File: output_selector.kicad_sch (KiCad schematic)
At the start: 0 parts

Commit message: power supply first draft
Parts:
- added U2: ATTINY9-TS8R, 0__:SOT95P270X145-6N, symbol 0 __:ATTINY9-TS8R
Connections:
- new net +5V: U2.5 (VCC)
- new net GND: U2.2 (GND)

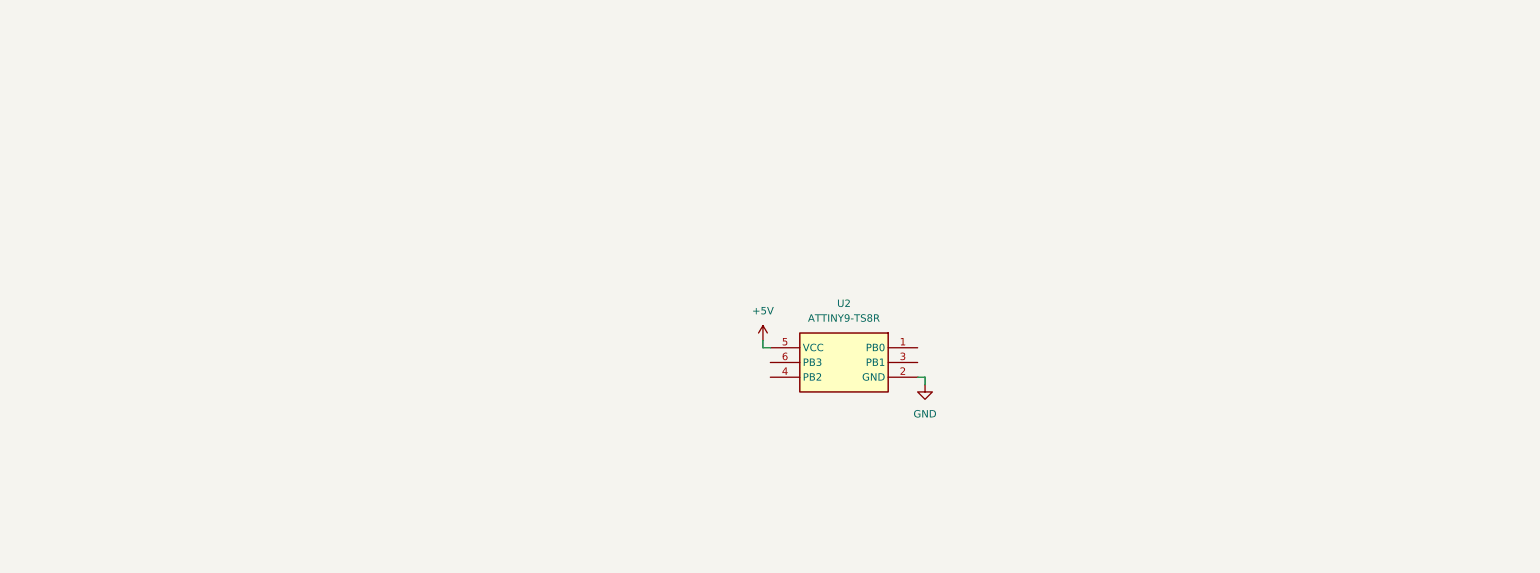
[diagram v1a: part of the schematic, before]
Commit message: Add output selector
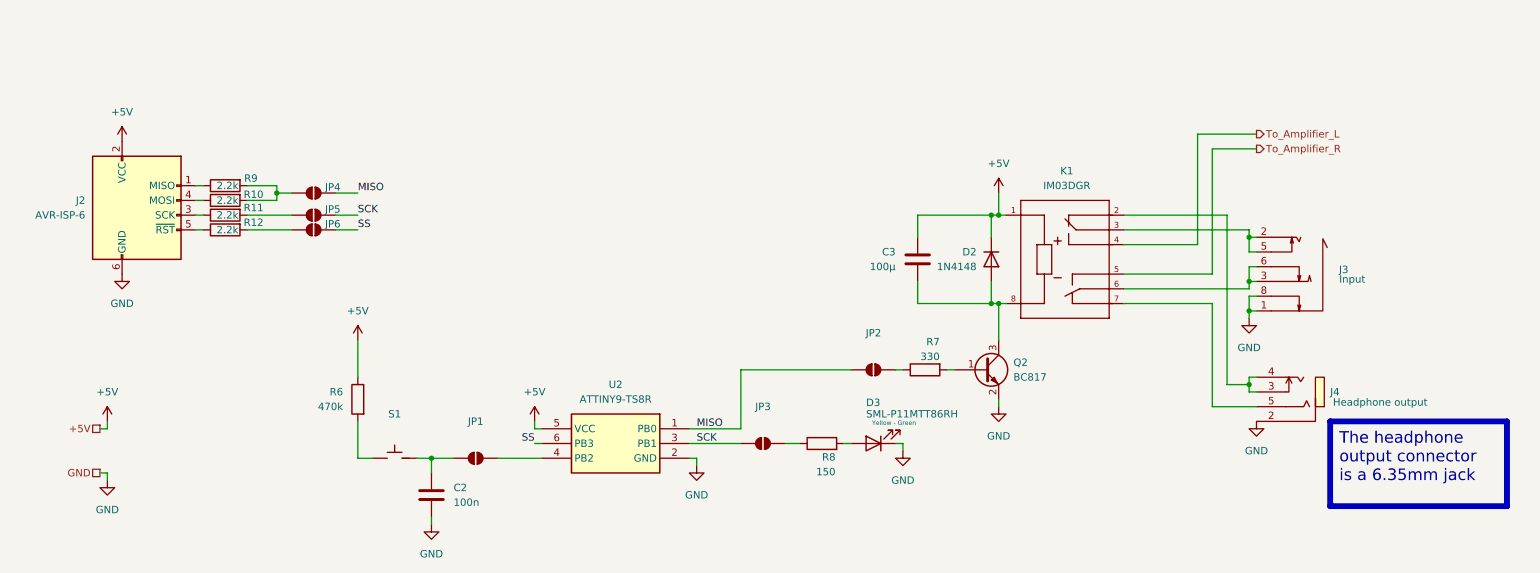
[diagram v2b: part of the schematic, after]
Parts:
- added C2: 100n, symbol Device:C
- added C3: 100µ, symbol Device:C
- added D2: 1N4148, Diode_THT:D_DO-35_SOD27_P7.62mm_Horizontal, symbol Diode:1N4148
- added D3: SML-P11MTT86RH, LED_SMD:LED_0402_1005Metric, symbol Device:LED
- added J2: AVR-ISP-6, symbol Connector:AVR-ISP-6
- added J3: PJ-393-8P, 0__:AUDIO-TH_PJ-393-8A, symbol 0 __:PJ-393-8P
- added J4: PJ-603, 0__:AUDIO-TH_PJ-603, symbol 0 __:PJ-603
- added JP1, JP2, JP3, JP4, JP5, JP6: SolderJumper_2_Open, Jumper:SolderJumper-2_P1.3mm_Open_TrianglePad1.0x1.5mm, symbol Jumper:SolderJumper_2_Open
- added K1: IM03DGR, 0__:RELAY_IM03DGR, symbol 0 __:IM03DGR
- added Q2: BC817, Package_TO_SOT_SMD:SOT-23, symbol Transistor_BJT:BC817
- added R10, R11, R12, R9: 2.2k, symbol Device:R
- added R6: 470k, symbol Device:R
- added R7: 330, symbol Device:R
- added R8: 150, symbol Device:R
- added S1: PG151101S11, 0__:SW_PG151101S11, symbol 0 __:PG151101S11
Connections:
- net +5V: now also C3.2, D2.1 (K), J2.2 (VCC), K1.1, R6.1
- net GND: now also C2.1, D3.1 (K), J2.6 (GND), J3.1, J3.8, J4.2, Q2.2 (E)
- net MISO: now reaches U2.1 (PB0)
- net MISO: now also JP2.1 (A), JP4.2 (B)
- net SCK: now reaches U2.3 (PB1)
- net SCK: now also JP3.1 (A), JP5.2 (B)
- net at U2.4 (PB2): now also JP1.2 (B)
- net SS: now reaches U2.6 (PB3)
- net SS: now also JP6.2 (B)
- new net: JP5.1 (A), R11.2
- new net: JP6.1 (A), R12.2
- new net: JP4.1 (A), R10.2, R9.2
- new net: C2.2, JP1.1 (A), S1.2
- new net: JP3.2 (B), R8.1
- new net: C3.1, D2.2 (A), K1.8, Q2.3 (C)
- new net: JP2.2 (B), R7.1
- new net: J2.4 (MOSI), R10.1
- new net: D3.2 (A), R8.2
- new net: Q2.1 (B), R7.2
- new net: J4.3, J4.4, K1.2
- new net: J3.2, J3.5, K1.3
- new net: J3.3, J3.6, K1.6
- new net: J4.5, K1.7
- new net: R6.2, S1.1
- new net: J2.3 (SCK), R11.1
- new net: J2.5 (~{RST}), R12.1
- new net: J2.1 (MISO), R9.1
- new net To_Amplifier_L: K1.4
- new net To_Amplifier_R: K1.5
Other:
- moved on the sheet: U2

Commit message: draft amplifier circuit
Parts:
- added JP7: SolderJumper_2_Open, Jumper:SolderJumper-2_P1.3mm_Open_TrianglePad1.0x1.5mm, symbol Jumper:SolderJumper_2_Open
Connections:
- net SS: now also JP7.2 (B)
- new net ~{AmpSD}: JP7.1 (A)
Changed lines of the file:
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@@
+	(wire
+		(pts
+			(xy 137.16 158.75) (xy 140.97 158.75)
+		)
+		(stroke
+			(width 0)
+			(type default)
+		)
+	)
 	(wire
 		(pts
@@
 	(wire
 		(pts
+			(xy 129.54 158.75) (xy 128.27 158.75)
+		)
+		(stroke
+			(width 0)
+			(type default)
+		)
+	)
+	(wire
+		(pts
 			(xy 66.04 154.94) (xy 66.04 156.21)
 		)
@@
 		(pts
 			(xy 219.71 134.62) (xy 219.71 140.97)
-		)
-		(stroke
-			(width 0)
-			(type default)
-		)
-	)
-	(wire
-		(pts
-			(xy 139.7 158.75) (xy 140.97 158.75)
 		)
 		(stroke
@@
 		(shape passive)
 		(at 64.77 163.83 180)
+		(fields_autoplaced yes)
+		(effects
+			(font
+				(size 1.27 1.27)
+			)
+			(justify right)
+		)
+	)
+	(hierarchical_label "~{AmpSD}"
+		(shape output)
+		(at 128.27 158.75 180)
 		(fields_autoplaced yes)
 		(effects
@@
 		(on_board yes)
 		(dnp no)
-		(fields_autoplaced yes)
 		(property "Reference" "JP1"
-			(at 129.54 154.94 0)
+			(at 129.54 163.576 0)
 			(effects
 				(font
@@
 					(unit 1)
 				)
+			)
+		)
+	)
+	(symbol
+		(lib_id "Jumper:SolderJumper_2_Open")
+		(at 133.35 158.75 0)
+		(unit 1)
+		(exclude_from_sim yes)
+		(in_bom no)
+		(on_board yes)
+		(dnp no)
+		(property "Reference" "JP7"
+			(at 133.35 156.21 0)
+			(effects
+				(font
+					(size 1.27 1.27)
+				)
+			)
+		)
+		(property "Value" "SolderJumper_2_Open"
+			(at 133.35 154.94 0)
+			(effects
+				(font
+					(size 1.27 1.27)
+				)
+				(hide yes)
+			)
+		)
+		(property "Footprint" "Jumper:SolderJumper-2_P1.3mm_Open_TrianglePad1.0x1.5mm"
+			(at 133.35 158.75 0)
+			(effects
+				(font
+					(size 1.27 1.27)
+				)
+				(hide yes)
+			)
+		)
+		(property "Datasheet" "~"
+			(at 133.35 158.75 0)
+			(effects
+				(font
+					(size 1.27 1.27)
+				)
+				(hide yes)
+			)
+		)
+		(property "Description" "Solder Jumper, 2-pole, open"
+			(at 133.35 158.75 0)
+			(effects
+				(font
+					(size 1.27 1.27)
+				)
+				(hide yes)
+			)
+		)
+		(pin "2"
+		)
+		(pin "1"
+		)
+		(instances
+			(project "AudioInterface"
+				(path "/0650c7a8-acba-429c-9f8e-eec0baf0bc1c/fede4c36-00cc-4d3d-b71c-5243ba232202/86fedcf6-4284-4ef9-aa8f-0fb0258e957c"
+					(reference "JP7")
+					(unit 1)
+				)

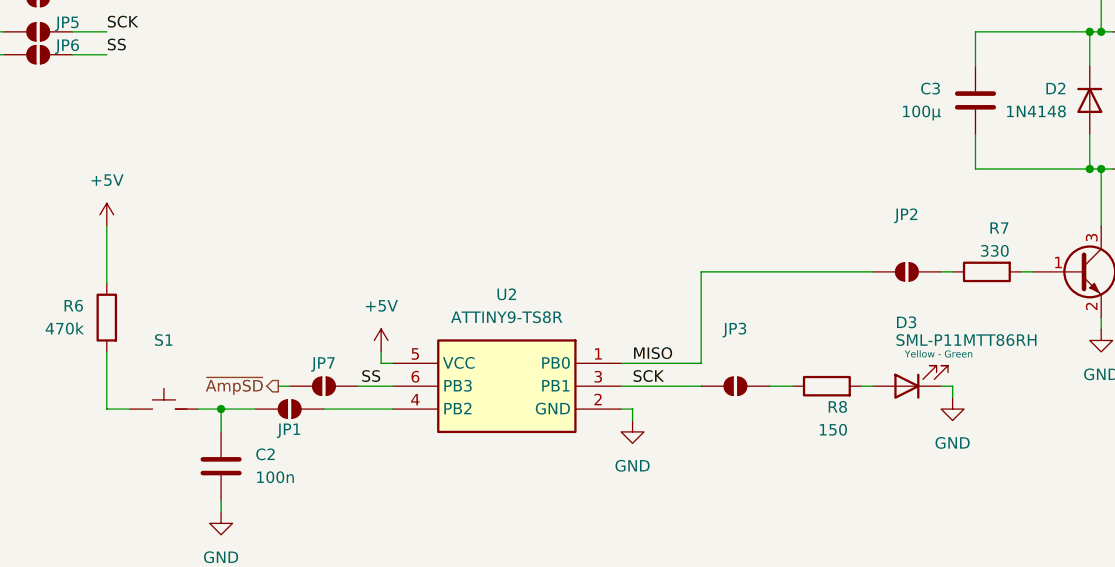
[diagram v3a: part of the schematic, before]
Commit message: Finish amplifier, add shutdown control
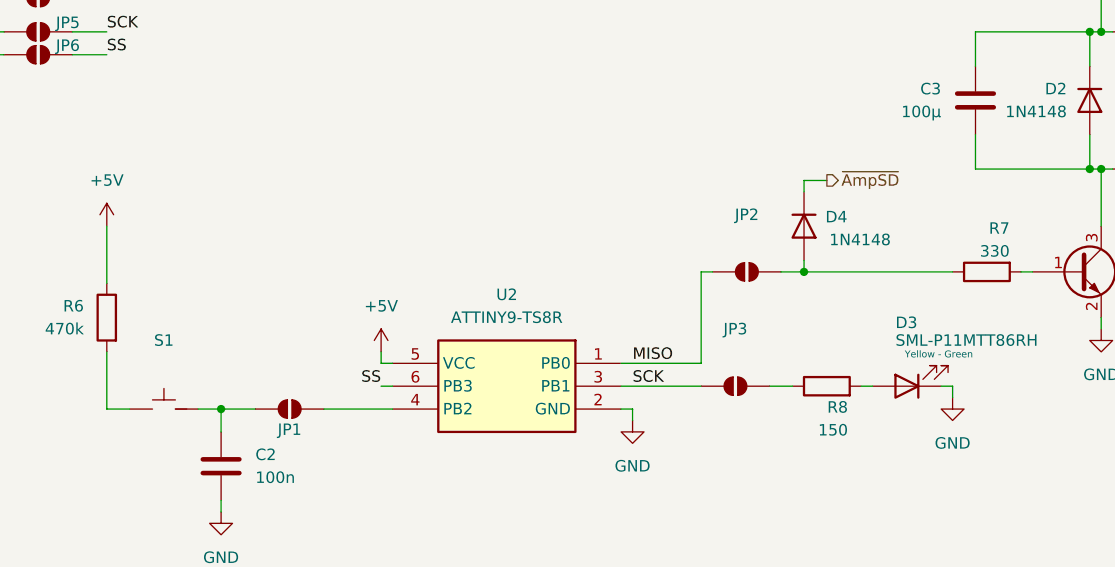
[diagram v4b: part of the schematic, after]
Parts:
- removed JP7: SolderJumper_2_Open, Jumper:SolderJumper-2_P1.3mm_Open_TrianglePad1.0x1.5mm, symbol Jumper:SolderJumper_2_Open
- added D4: 1N4148, Diode_THT:D_DO-35_SOD27_P7.62mm_Horizontal, symbol Diode:1N4148
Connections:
- net ~{AmpSD}: now also D4.1 (K)
- net at JP2.2 (B), R7.1: now also D4.2 (A)
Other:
- moved on the sheet: JP2
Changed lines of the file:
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@@
 	)
 	(junction
+		(at 186.69 146.05)
+		(diameter 0)
+		(color 0 0 0 0)
+	)
+	(junction
 		(at 218.44 119.38)
 		(diameter 0)
@@
 	(wire
 		(pts
-			(xy 137.16 158.75) (xy 140.97 158.75)
-		)
-		(stroke
-			(width 0)
-			(type default)
-		)
-	)
-	(wire
-		(pts
 			(xy 256.54 107.95) (xy 264.16 107.95)
 		)
@@
 	(wire
 		(pts
+			(xy 139.7 158.75) (xy 140.97 158.75)
+		)
+		(stroke
+			(width 0)
+			(type default)
+		)
+	)
+	(wire
+		(pts
 			(xy 95.25 114.3) (xy 95.25 115.57)
 		)
@@
 	(wire
 		(pts
+			(xy 189.23 135.89) (xy 186.69 135.89)
+		)
+		(stroke
+			(width 0)
+			(type default)
+		)
+	)
+	(wire
+		(pts
 			(xy 219.71 119.38) (xy 220.98 119.38)
 		)
@@
 	(wire
 		(pts
-			(xy 129.54 158.75) (xy 128.27 158.75)
-		)
-		(stroke
-			(width 0)
-			(type default)
-		)
-	)
-	(wire
-		(pts
 			(xy 66.04 154.94) (xy 66.04 156.21)
 		)
@@
 	(wire
 		(pts
+			(xy 186.69 144.78) (xy 186.69 146.05)
+		)
+		(stroke
+			(width 0)
+			(type default)
+		)
+	)
+	(wire
+		(pts
 			(xy 264.16 125.73) (xy 262.89 125.73)
 		)
@@
 	(wire
 		(pts
+			(xy 186.69 146.05) (xy 203.2 146.05)
+		)
+		(stroke
+			(width 0)
+			(type default)
+		)
+	)
+	(wire
+		(pts
 			(xy 166.37 158.75) (xy 175.26 158.75)
 		)
@@
 	(wire
 		(pts
-			(xy 175.26 146.05) (xy 194.31 146.05)
+			(xy 175.26 146.05) (xy 176.53 146.05)
 		)
 		(stroke
@@
 	(wire
 		(pts
-			(xy 201.93 146.05) (xy 203.2 146.05)
+			(xy 184.15 146.05) (xy 186.69 146.05)
 		)
 		(stroke
@@
 	(wire
 		(pts
+			(xy 186.69 135.89) (xy 186.69 137.16)
+		)
+		(stroke
+			(width 0)
+			(type default)
+		)
+	)
+	(wire
+		(pts
 			(xy 111.76 161.29) (xy 109.22 161.29)
 		)
@@
 	(hierarchical_label "~{AmpSD}"
 		(shape output)
-		(at 128.27 158.75 180)
+		(at 189.23 135.89 0)
 		(fields_autoplaced yes)
 		(effects
@@
 				(size 1.27 1.27)
 			)
-			(justify right)
+			(justify left)
 		)
 	)
@@
 	)
 	(symbol
+		(lib_id "Diode:1N4148")
+		(at 186.69 140.97 270)
+		(unit 1)
+		(exclude_from_sim no)
+		(in_bom yes)
+		(on_board yes)
+		(dnp no)
+		(property "Reference" "D4"
+			(at 191.516 139.954 90)
+			(effects
+				(font
+					(size 1.27 1.27)
+				)
+				(justify right)
+			)
+		)
+		(property "Value" "1N4148"
+			(at 196.342 142.494 90)
+			(effects
+				(font
+					(size 1.27 1.27)
+				)
+				(justify right)
+			)
+		)
+		(property "Footprint" "Diode_THT:D_DO-35_SOD27_P7.62mm_Horizontal"
+			(at 186.69 140.97 0)
+			(effects
+				(font
+					(size 1.27 1.27)
+				)
+				(hide yes)
+			)
+		)
+		(property "Datasheet" "https://assets.nexperia.com/documents/data-sheet/1N4148_1N4448.pdf"
+			(at 186.69 140.97 0)
+			(effects
+				(font
+					(size 1.27 1.27)
+				)
+				(hide yes)
+			)
+		)
+		(property "Description" "100V 0.15A standard switching diode, DO-35"
+			(at 186.69 140.97 0)
+			(effects
+				(font
+					(size 1.27 1.27)
+				)
+				(hide yes)
+			)
+		)
+		(property "Sim.Device" "D"
+			(at 186.69 140.97 0)
+			(effects
+				(font
+					(size 1.27 1.27)
+				)
+				(hide yes)
+			)
+		)
+		(property "Sim.Pins" "1=K 2=A"
+			(at 186.69 140.97 0)
+			(effects
+				(font
+					(size 1.27 1.27)
+				)
+				(hide yes)
+			)
+		)
+		(pin "1"
+		)
+		(pin "2"
+		)
+		(instances
+			(project "AudioInterface"
+				(path "/0650c7a8-acba-429c-9f8e-eec0baf0bc1c/fede4c36-00cc-4d3d-b71c-5243ba232202/86fedcf6-4284-4ef9-aa8f-0fb0258e957c"
+					(reference "D4")
+					(unit 1)
+				)
+			)
+		)
+	)
+	(symbol
 		(lib_id "power:GND")
 		(at 219.71 152.4 0)
@@
 	(symbol
 		(lib_id "Jumper:SolderJumper_2_Open")
-		(at 198.12 146.05 0)
+		(at 180.34 146.05 0)
 		(unit 1)
 		(exclude_from_sim yes)
@@
 		(fields_autoplaced yes)
 		(property "Reference" "JP2"
-			(at 198.12 139.7 0)
+			(at 180.34 139.7 0)
 			(effects
 				(font
@@
 		)
 		(property "Value" "SolderJumper_2_Open"
-			(at 198.12 142.24 0)
+			(at 180.34 142.24 0)
 			(effects
 				(font
@@
 		)
 		(property "Footprint" "Jumper:SolderJumper-2_P1.3mm_Open_TrianglePad1.0x1.5mm"
-			(at 198.12 146.05 0)
+			(at 180.34 146.05 0)
 			(effects
 				(font
@@
 		)
 		(property "Datasheet" "~"
-			(at 198.12 146.05 0)
+			(at 180.34 146.05 0)
 			(effects
 				(font
@@
 		)
 		(property "Description" "Solder Jumper, 2-pole, open"
-			(at 198.12 146.05 0)
+			(at 180.34 146.05 0)
 			(effects
 				(font
@@
 					(unit 1)
 				)
-			)
-		)
-	)
-	(symbol
-		(lib_id "Jumper:SolderJumper_2_Open")
-		(at 133.35 158.75 0)
-		(unit 1)
-		(exclude_from_sim yes)
-		(in_bom no)
-		(on_board yes)
-		(dnp no)
-		(property "Reference" "JP7"
-			(at 133.35 156.21 0)
-			(effects
-				(font
-					(size 1.27 1.27)
-				)
-			)
-		)
-		(property "Value" "SolderJumper_2_Open"
-			(at 133.35 154.94 0)
-			(effects
-				(font
-					(size 1.27 1.27)
-				)
-				(hide yes)
-			)
-		)
-		(property "Footprint" "Jumper:SolderJumper-2_P1.3mm_Open_TrianglePad1.0x1.5mm"
-			(at 133.35 158.75 0)
-			(effects
-				(font
-					(size 1.27 1.27)
-				)
-				(hide yes)
-			)
-		)
-		(property "Datasheet" "~"
-			(at 133.35 158.75 0)
-			(effects
-				(font
-					(size 1.27 1.27)
-				)
-				(hide yes)
-			)
-		)
-		(property "Description" "Solder Jumper, 2-pole, open"
-			(at 133.35 158.75 0)
-			(effects
-				(font
-					(size 1.27 1.27)
-				)
-				(hide yes)
-			)
-		)
-		(pin "2"
-		)
-		(pin "1"
-		)
-		(instances
-			(project "AudioInterface"
-				(path "/0650c7a8-acba-429c-9f8e-eec0baf0bc1c/fede4c36-00cc-4d3d-b71c-5243ba232202/86fedcf6-4284-4ef9-aa8f-0fb0258e957c"
-					(reference "JP7")
-					(unit 1)
-				)
